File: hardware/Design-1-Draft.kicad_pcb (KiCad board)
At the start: 2 copper layers, 32 parts, among them J1 Barrel_Jack_Switch, M1 WATERPUMP-1, M2 WATERPUMP-2, Q1 IRLZ44N, Q2 IRLZ44N, SW1 Button, U3 ADS1115IDGS, U5 Tang_Nano_9K

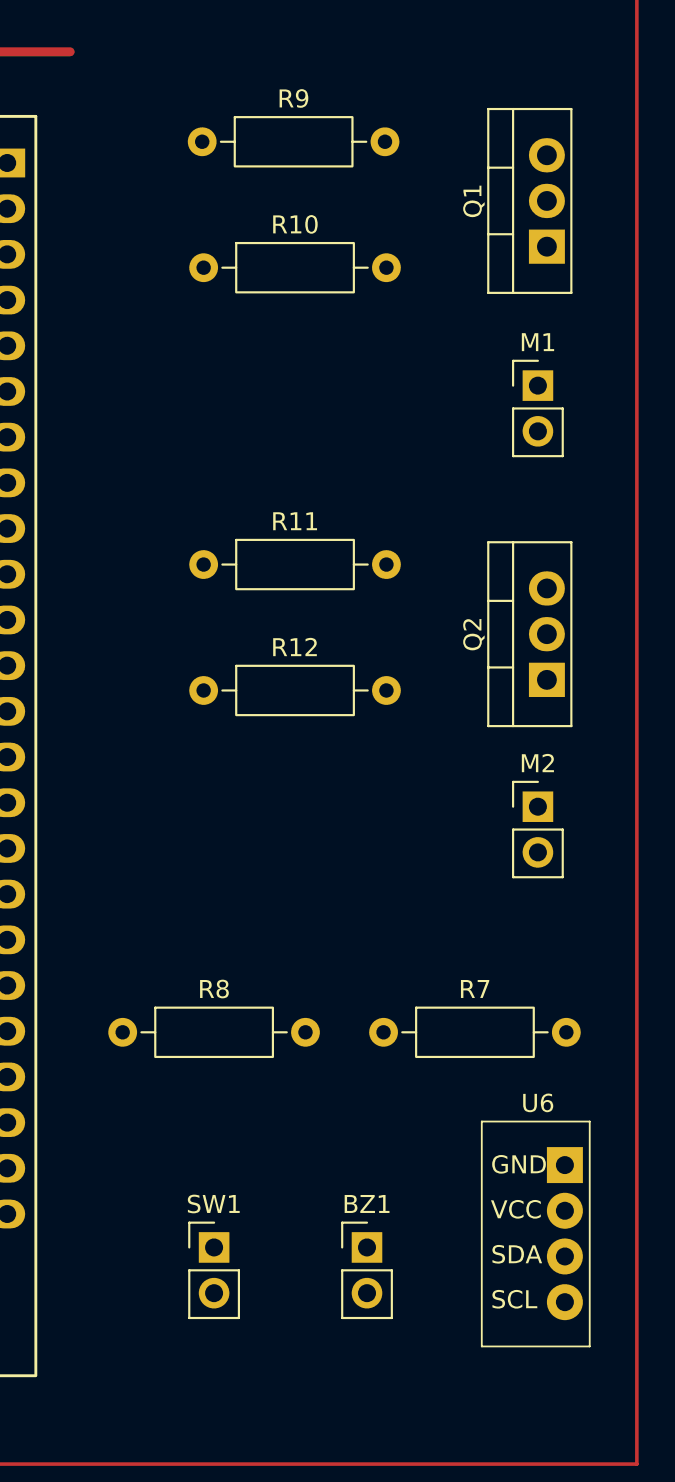
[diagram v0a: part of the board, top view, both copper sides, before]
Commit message: fixed footprint text
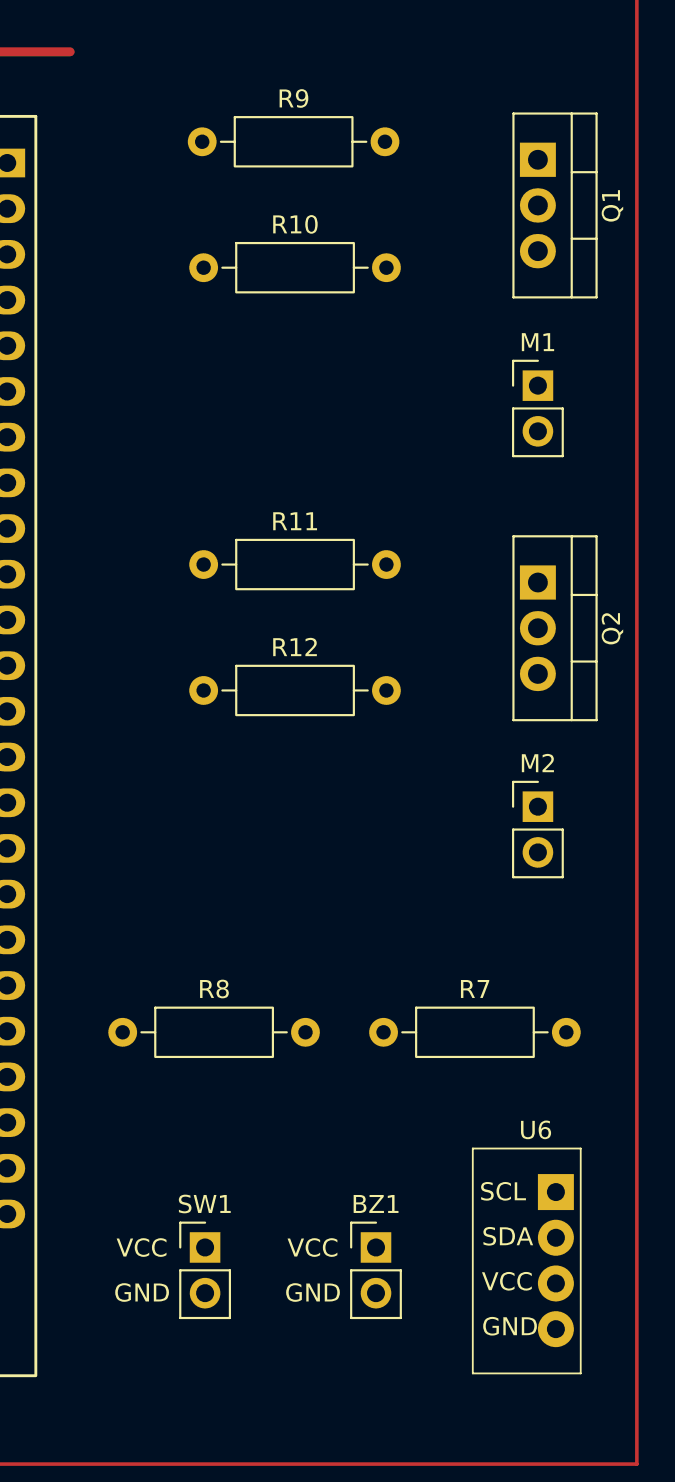
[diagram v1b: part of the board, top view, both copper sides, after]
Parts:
- moved Q2 5.43 mm to (178.5, 84.5), turned to -90 degrees
- moved Q1 4.86 mm to (178.5, 61.0), turned to -90 degrees
- moved U6 1.58 mm to (178.0, 122.2)
- moved BZ1 0.50 mm to (169.5, 121.5)
- moved SW1 0.50 mm to (160.0, 121.5)
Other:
- board text added: "GND"
- board text added: "VCC"

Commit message: added some traces
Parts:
- moved U4 4.50 mm to (151.4, 43.3)
- moved U5 4.00 mm to (133.6, 90.4)
- moved C5 2.06 mm to (114.0, 54.5)
- moved R11 2.00 mm to (159.9, 81.5)
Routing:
- net Net-(D1-K): track 50.4 -> 154.7 mm, vias 0 -> 1
- net Net-(Q2-G): track 0.00 -> 25.8 mm
- net Net-(BZ1-+): track 0.00 -> 19.6 mm
- net GND: track 0.00 -> 8.80 mm
- net (no net): track 0.00 -> 2.00 mm

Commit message: updated schematic and pcb
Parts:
- U3: footprint Package_SO:TSSOP-10_3x3mm_P0.5mm -> 1_CustomFootprints:ADS1115
- moved J1 86.3 mm to (81.7, 126.8)
- moved D1 86.1 mm to (132.1, 126.5)
- moved F1 86.0 mm to (89.5, 126.5)
- moved BZ1 81.2 mm to (180.5, 41.0)
- moved U4 78.7 mm to (153.2, 122.0)
- moved U6 70.1 mm to (168.8, 52.7)
- moved R7 69.4 mm to (160.6, 40.8)
- moved SW1 63.5 mm to (178.8, 60.8)
- moved C5 62.7 mm to (126.0, 116.0)
- moved R8 45.4 mm to (159.1, 64.2)
- moved R6 29.1 mm to (101.8, 74.5)
- moved C4 28.9 mm to (111.5, 96.2), turned to 180 degrees
- moved R1 26.0 mm to (101.0, 41.0), turned to 180 degrees
- moved U1 24.8 mm to (76.0, 44.2)
- moved C1 24.0 mm to (93.5, 54.5)
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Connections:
- R11 pad 1: Net-(U5-70_IOT41B) -> Net-(U5-31_IOB15A)
- R8 pad 1: Net-(U5-72_IOT39B) -> Net-(U5-77_IOT37A)
- R8 pad 2: Net-(U5-73_IOT39A) -> Net-(U5-79_IOT12B_1V8)
- R9 pad 1: Net-(U5-71_IOT41A) -> Net-(U5-74_IOT38B)
- SW1 pad 1: Net-(U5-73_IOT39A) -> Net-(U5-79_IOT12B_1V8)
- U5 pad 28: unconnected-(U5-31_IOB15A-Pad28) -> Net-(U5-31_IOB15A)
- U5 pad 32: Net-(U5-70_IOT41B) -> unconnected-(U5-70_IOT41B-Pad32)
- U5 pad 33: Net-(U5-71_IOT41A) -> unconnected-(U5-71_IOT41A-Pad33)
- U5 pad 34: Net-(U5-72_IOT39B) -> unconnected-(U5-72_IOT39B-Pad34)
- U5 pad 35: Net-(U5-73_IOT39A) -> unconnected-(U5-73_IOT39A-Pad35)
- U5 pad 36: unconnected-(U5-74_IOT38B-Pad36) -> Net-(U5-74_IOT38B)
- U5 pad 39: unconnected-(U5-77_IOT37A-Pad39) -> Net-(U5-77_IOT37A)
- U5 pad 40: unconnected-(U5-79_IOT12B_1V8-Pad40) -> Net-(U5-79_IOT12B_1V8)
- U5 pad 42: Net-(U5-81_IOT11B_1V8) -> unconnected-(U5-81_IOT11B_1V8-Pad42)
- U5 pad 43: Net-(U5-82_IOT11A_1V8) -> unconnected-(U5-82_IOT11A_1V8-Pad43)
- U5 pad 44: unconnected-(U5-83_IOT10B_1V8-Pad44) -> Net-(U5-83_IOT10B_1V8)
- U5 pad 45: unconnected-(U5-84_IOT10A_1V8-Pad45) -> Net-(U5-84_IOT10A_1V8)
- U6 pad 1: Net-(U5-82_IOT11A_1V8) -> Net-(U5-84_IOT10A_1V8)
- U6 pad 2: Net-(U5-81_IOT11B_1V8) -> Net-(U5-83_IOT10B_1V8)
- U6 pad 3: Net-(U3-VDD) -> Net-(D1-K)
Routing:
- net Net-(U3-VDD): track 0.00 -> 194.5 mm
- net Net-(D1-K): track 154.7 -> 334.0 mm, vias 1 -> 0
- net Net-(U3-AIN1): track 0.00 -> 102.2 mm
- net Net-(U3-AIN0): track 0.00 -> 72.3 mm
- net Net-(U3-ALERT/RDY): track 0.00 -> 69.0 mm
- net Net-(U3-SCL): track 0.00 -> 54.2 mm, vias 0 -> 1
- net Net-(U5-79_IOT12B_1V8): track 0.00 -> 41.4 mm
- net Net-(U3-SDA): track 0.00 -> 39.6 mm, vias 0 -> 2
- net Net-(U5-84_IOT10A_1V8): track 0.00 -> 28.3 mm
- net Net-(U5-83_IOT10B_1V8): track 0.00 -> 28.3 mm
- net Net-(U2-A0): track 0.00 -> 20.1 mm
- net Net-(Q1-G): track 0.00 -> 19.2 mm
- net Net-(U5-63_IOR5A): track 0.00 -> 18.4 mm
- net Net-(U5-31_IOB15A): track 0.00 -> 18.1 mm
- net Net-(M2--): track 0.00 -> 17.3 mm
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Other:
- board outline added: 120 x 100 mm

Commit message: updated schematic and pcb
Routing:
- net Net-(D1-K): track 334.0 -> 336.5 mm
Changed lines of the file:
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@@
+	)
+	(segment
+		(start 143 129.112)
+		(end 143 126.572)
+		(width 0.2)
+		(layer "F.Cu")
+		(net 5)
 	)
 	(segment

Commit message: updated pcb
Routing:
- net Net-(U3-VDD): track 194.5 -> 200.3 mm
- net Net-(D1-K): track 336.5 -> 340.5 mm
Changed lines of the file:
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@@
 	(segment
 		(start 165.301 126.699)
-		(end 166 126)
+		(end 165.5 126.5)
 		(width 0.2)
 		(layer "F.Cu")
@@
 	)
 	(segment
+		(start 161.796 129.239)
+		(end 164.511 129.239)
+		(width 0.2)
+		(layer "F.Cu")
+		(net 4)
+	)
+	(segment
 		(start 148 100)
 		(end 147 99)
@@
 	)
 	(segment
+		(start 165.25 126.75)
+		(end 165.5 126.5)
+		(width 0.2)
+		(layer "F.Cu")
+		(net 4)
+	)
+	(segment
 		(start 112.5 91.5)
 		(end 102.25 91.5)
@@
 	)
 	(segment
+		(start 165.25 128.5)
+		(end 165.25 126.75)
+		(width 0.2)
+		(layer "F.Cu")
+		(net 4)
+	)
+	(segment
 		(start 101.6 81)
 		(end 101.6 83.9)
@@
 	)
 	(segment
+		(start 164.511 129.239)
+		(end 165.25 128.5)
+		(width 0.2)
+		(layer "F.Cu")
+		(net 4)
+	)
+	(segment
 		(start 142.2569 99)
 		(end 142.1969 99.06)
@@
 	)
 	(segment
+		(start 165.5 126.5)
+		(end 166 126)
+		(width 0.2)
+		(layer "F.Cu")
+		(net 4)
+	)
+	(segment
 		(start 115 89)
 		(end 112.5 91.5)
@@
 	)
 	(segment
-		(start 143 129.112)
-		(end 143 126.572)
-		(width 0.2)
-		(layer "F.Cu")
-		(net 5)
-	)
-	(segment
 		(start 87.25 88.25)
 		(end 87.25 41.25)
@@
 	(segment
 		(start 135.5 126.5)
-		(end 142.928 126.5)
+		(end 137.5 126.5)
 		(width 1.5)
 		(layer "B.Cu")
@@
 	)
 	(segment
+		(start 137.75 126.5)
+		(end 140.362 129.112)
+		(width 1.5)
+		(layer "B.Cu")
+		(net 5)
+	)
+	(segment
 		(start 84 38)
 		(end 78.05 38)
@@
 	)
 	(segment
+		(start 137.5 126.5)
+		(end 142.928 126.5)
+		(width 1.5)
+		(layer "B.Cu")
+		(net 5)
+	)
+	(segment
 		(start 83.5 108.5)
 		(end 83.5 103.72)
@@
 	)
 	(segment
+		(start 140.362 129.112)
+		(end 143 129.112)
+		(width 1.5)
+		(layer "B.Cu")
+		(net 5)
+	)
+	(segment
 		(start 137 114)
 		(end 135.75 112.75)
@@
 		(width 1.5)
 		(layer "B.Cu")
+		(net 5)
+	)
+	(segment
+		(start 137.5 126.5)
+		(end 137.75 126.5)
+		(width 1.5)
+		(layer "B.Cu")

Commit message: updated pcb
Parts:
- moved C1 2.00 mm to (91.5, 54.5)
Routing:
- net Net-(U3-ALERT/RDY): track 69.0 -> 58.9 mm
- net Net-(U3-VDD): track 200.3 -> 201.8 mm
- net Net-(U3-AIN0): track 72.3 -> 73.3 mm

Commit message: updated PCB
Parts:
- moved C5 8.51 mm to (118.1, 119.2)
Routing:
- net Net-(U4-IN-): track 0.00 -> 80.0 mm
- net Net-(D1-K): track 340.5 -> 348.1 mm, vias 0 -> 1
- net Net-(Q2-G): track 20.9 -> 19.5 mm
- added copper zone on B.Cu, net GND
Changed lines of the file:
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@@
 	(footprint "Capacitor_THT:CP_Radial_D10.0mm_P5.00mm"
 		(layer "F.Cu")
-		(at 126 116)
+		(at 118.132323 119.25)
 		(descr "CP, Radial series, Radial, pin pitch=5.00mm, diameter=10mm, height=16mm, Electrolytic Capacitor")
 		(tags "CP Radial series Radial pin pitch 5.00mm diameter 10mm height 16mm Electrolytic Capacitor")
 		(property "Reference" "C5"
-			(at 2.5 -6.25 0)
+			(at -4.882323 0.25 0)
 			(layer "F.SilkS")
 			(effects
@@
 	)
 	(segment
+		(start 123.132323 119.25)
+		(end 136.75 119.25)
+		(width 0.2)
+		(layer "F.Cu")
+		(net 5)
+	)
+	(segment
+		(start 136.75 119.25)
+		(end 137 119.5)
+		(width 0.2)
+		(layer "F.Cu")
+		(net 5)
+	)
+	(via
+		(at 137 119.5)
+		(size 0.6)
+		(drill 0.3)
+		(layers "F.Cu" "B.Cu")
+		(net 5)
+	)
+	(segment
 		(start 87.25 88.25)
 		(end 87.25 41.25)
@@
 	)
 	(segment
+		(start 137 125)
+		(end 135.5 126.5)
+		(width 2)
+		(layer "B.Cu")
+		(net 5)
+	)
+	(segment
 		(start 135.75 112.75)
 		(end 87.75 112.75)
@@
 	)
 	(segment
-		(start 137 117)
-		(end 136 116)
-		(width 2)
-		(layer "B.Cu")
-		(net 5)
-	)
-	(segment
 		(start 78.05 38)
 		(end 78 38.05)
@@
 	)
 	(segment
+		(start 137 119.5)
+		(end 137 120.5)
+		(width 2)
+		(layer "B.Cu")
+		(net 5)
+	)
+	(segment
 		(start 83.5 103.72)
 		(end 81.5 101.72)
@@
 	)
 	(segment
-		(start 137 117)
+		(start 137 119.5)
 		(end 137 114)
 		(width 2)
@@
 	)
 	(segment
-		(start 83.5 92)
-		(end 87.25 88.25)
-		(width 2)
-		(layer "B.Cu")
-		(net 5)
-	)
-	(segment
-		(start 136 116)
-		(end 131 116)
+		(start 137 120.5)
+		(end 137 125)
 		(width 2)
 		(layer "B.Cu")
@@
 	)
 	(segment
-		(start 137 125)
-		(end 137 117)
+		(start 83.5 92)
+		(end 87.25 88.25)
 		(width 2)
 		(layer "B.Cu")
@@
 	)
 	(segment
-		(start 135.5 126.5)
-		(end 137 125)
-		(width 2)
-		(layer "B.Cu")
-		(net 5)
-	)
-	(segment
 		(start 87.75 112.75)
 		(end 83.5 108.5)
@@
 	(segment
 		(start 175 96.92)
-		(end 175.25 96.92)
-		(width 0.2)
-		(layer "F.Cu")
-		(net 9)
-	)
-	(segment
-		(start 175 96.92)
-		(end 174.17 97.75)
-		(width 0.2)
-		(layer "F.Cu")
-		(net 9)
-	)
-	(segment
-		(start 175 96.92)
 		(end 173.17 96.92)
 		(width 0.8)
@@
 	)
 	(segment
-		(start 172.92 99)
-		(end 175 96.92)
+		(start 170.25 99)
+		(end 172.92 99)
 		(width 0.8)
 		(layer "F.Cu")
@@
 	)
 	(segment
-		(start 170.25 99)
-		(end 172.92 99)
+		(start 171.92 95.67)
+		(end 168.75 95.67)
 		(width 0.8)
 		(layer "F.Cu")
@@
 	)
 	(segment
-		(start 171.92 95.67)
-		(end 168.75 95.67)
+		(start 172.92 99)
+		(end 175 96.92)
+		(width 0.8)
+		(layer "F.Cu")
+		(net 9)
+	)
+	(segment
+		(start 168.75 100.5)
+		(end 170.25 99)
 		(width 0.8)
 		(layer "F.Cu")
@@
 	)
 	(segment
-		(start 168.75 100.5)
-		(end 170.25 99)
-		(width 0.8)
-		(layer "F.Cu")
-		(net 9)
-	)
-	(segment
 		(start 174.55 111.45)
 		(end 171.5 111.45)
@@
 	)
 	(segment
+		(start 75.7 117.3)
+		(end 77.223 115.777)
+		(width 2)
+		(layer "F.Cu")
+		(net 51)
+	)
+	(segment
+		(start 143 115.777)
+		(end 143 118.2916)
+		(width 2)
+		(layer "F.Cu")
+		(net 51)
+	)
+	(segment
+		(start 77.223 115.777)
+		(end 143 115.777)
+		(width 2)
+		(layer "F.Cu")
+		(net 51)
+	)
+	(segment
+		(start 143 118.2916)
+		(end 142.9746 118.317)
+		(width 0.2)
+		(layer "F.Cu")
+		(net 51)
+	)
+	(segment
+		(start 75.7 126.75)
+		(end 75.7 117.3)
+		(width 2)
+		(layer "F.Cu")
+		(net 51)
+	)
+	(segment
+		(start 142.9746 115.8024)
+		(end 143 115.777)
+		(width 0.2)
+		(layer "B.Cu")
+		(net 51)
+	)
+	(segment
+		(start 142.9746 118.317)
+		(end 142.9746 118.2754)
+		(width 0.2)
+		(layer "B.Cu")
+		(net 51)
+	)
+	(segment
+		(start 142.9746 118.2754)
+		(end 143 118.25)
+		(width 0.2)
+		(layer "B.Cu")
+		(net 51)
+	)
+	(segment
 		(start 81.7 126.75)
 		(end 89.25 126.75)
@@
 		(net 67)
 	)
+	(zone
+		(net 1)
+		(net_name "GND")
+		(layer "B.Cu")
+		(hatch edge 0.5)
+		(connect_pads
+			(clearance 0.5)
+		)
+		(min_thickness 0.25)
+		(filled_areas_thickness no)
+		(fill yes
+			(thermal_gap 0.5)
+			(thermal_bridge_width 0.5)
+		)
+		(polygon
+			(pts
+				(xy 62 31.75) (xy 62.25 139) (xy 192 139.75) (xy 192 31.75)
+			)
+		)
+	)
 	(group ""

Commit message: updated PCB
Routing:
- net Net-(D1-K): track 348.1 -> 348.9 mm
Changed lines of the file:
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@@
+	)
+	(segment
+		(start 125.382323 121.5)
+		(end 137 121.5)
+		(width 0.8)
+		(layer "F.Cu")
+		(net 5)
 	)
 	(segment
 		(start 123.132323 119.25)
-		(end 136.75 119.25)
-		(width 0.2)
+		(end 125.382323 121.5)
+		(width 0.8)
 		(layer "F.Cu")
 		(net 5)
 	)
-	(segment
-		(start 136.75 119.25)
-		(end 137 119.5)
-		(width 0.2)
-		(layer "F.Cu")
-		(net 5)
-	)
 	(via
-		(at 137 119.5)
+		(at 137 121.5)
 		(size 0.6)
 		(drill 0.3)
@@
 	)
 	(segment
+		(start 137 120.5)
+		(end 137 121.5)
+		(width 2)
+		(layer "B.Cu")
+		(net 5)
+	)
+	(segment
 		(start 137 125)
 		(end 135.5 126.5)
@@
 	)
 	(segment
-		(start 137 120.5)
+		(start 137 121.5)
 		(end 137 125)
 		(width 2)
